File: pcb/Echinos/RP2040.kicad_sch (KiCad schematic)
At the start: 30 parts, among them J2 TagConnect_6pins, SW1 SW_Push, SW2 SW_Push, U2 RP2040, U2 W25Q128JVS, X1 ASE-12MHz

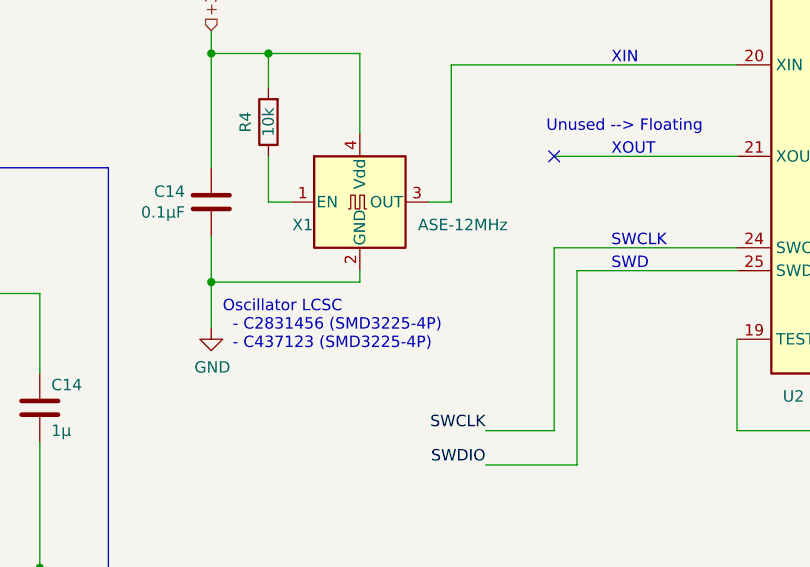
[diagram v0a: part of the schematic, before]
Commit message: ♻️ [PCB] - Fill / Check LCSC part number. Still some parts without a number:   - FPC connectors   - SATA connector   - Reset / Bootloader switches   - LED
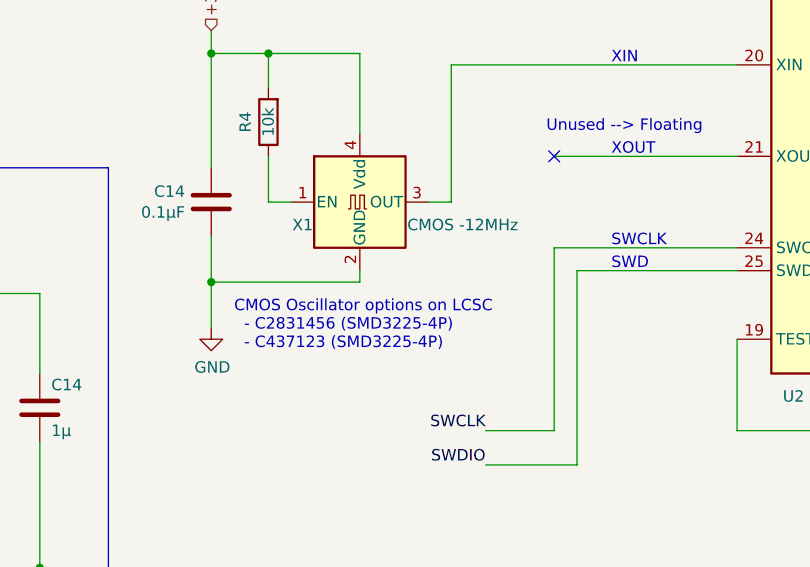
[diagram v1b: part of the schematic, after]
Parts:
- C14: LCSC TODO -> C5139511
- C14, C16: LCSC C19666 -> C458913
- R13: LCSC (none) -> C25744
- X1: value ASE-12MHz -> CMOS -12MHz; LCSC TODO -> C437123
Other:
- note added: "CMOS Oscillator options on LCSC - C2831456 (SMD3225-4P) - C437123 (SMD3225-4P)"
- note removed: "Oscillator LCSC - C2831456 (SMD3225-4P) - C437123 (SMD3225-4P)"
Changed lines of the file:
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@@
     (effects (font (size 1.27 1.27)) (justify right bottom))
   )
-  (text "Oscillator LCSC\n  - C2831456 (SMD3225-4P)\n  - C437123 (SMD3225-4P)"
-    (at 114.3 147.32 0)
+  (text "CMOS Oscillator options on LCSC\n  - C2831456 (SMD3225-4P)\n  - C437123 (SMD3225-4P)"
+    (at 115.57 147.32 0)
     (effects (font (size 1.27 1.27)) (justify left bottom))
   )
@@
       (effects (font (size 1.27 1.27)) hide)
     )
-    (property "LCSC" "C19666" (at 234.95 45.72 0)
+    (property "LCSC" "C458913" (at 234.95 45.72 0)
       (effects (font (size 1.27 1.27)) hide)
     )
@@
       (effects (font (size 1.27 1.27)) hide)
     )
-    (property "LCSC" "TODO" (at 113.03 130.81 0)
+    (property "LCSC" "C5139511" (at 113.03 130.81 0)
       (effects (font (size 1.27 1.27)) hide)
     )
@@
       (effects (font (size 1.27 1.27)) hide)
     )
-    (property "LCSC" "" (at 274.32 93.98 0)
+    (property "LCSC" "C25744" (at 274.32 93.98 0)
       (effects (font (size 1.27 1.27)) hide)
     )
@@
       (effects (font (size 1.27 1.27)) hide)
     )
-    (property "LCSC" "C19666" (at 170.18 46.99 0)
+    (property "LCSC" "C458913" (at 170.18 46.99 0)
       (effects (font (size 1.27 1.27)) hide)
     )
@@
       (effects (font (size 1.27 1.27)))
     )
-    (property "Value" "ASE-12MHz" (at 140.97 133.35 0)
+    (property "Value" "CMOS -12MHz" (at 140.97 133.35 0)
       (effects (font (size 1.27 1.27)))
     )
@@
       (effects (font (size 1.27 1.27)) hide)
     )
-    (property "Datasheet" "http://www.abracon.com/Oscillators/ASV.pdf" (at 127 130.81 0)
-      (effects (font (size 1.27 1.27)) hide)
-    )
-    (property "LCSC" "TODO" (at 129.54 130.81 0)
-      (effects (font (size 1.27 1.27)) hide)
-    )
+    (property "Datasheet" "https://datasheet.lcsc.com/lcsc/2304140030_JGHC-O3212000153350_C437123.pdf" (at 127 130.81 0)
+      (effects (font (size 1.27 1.27)) hide)
+    )
+    (property "LCSC" "C437123" (at 129.54 130.81 0)
+      (effects (font (size 1.27 1.27)) hide)
+    )

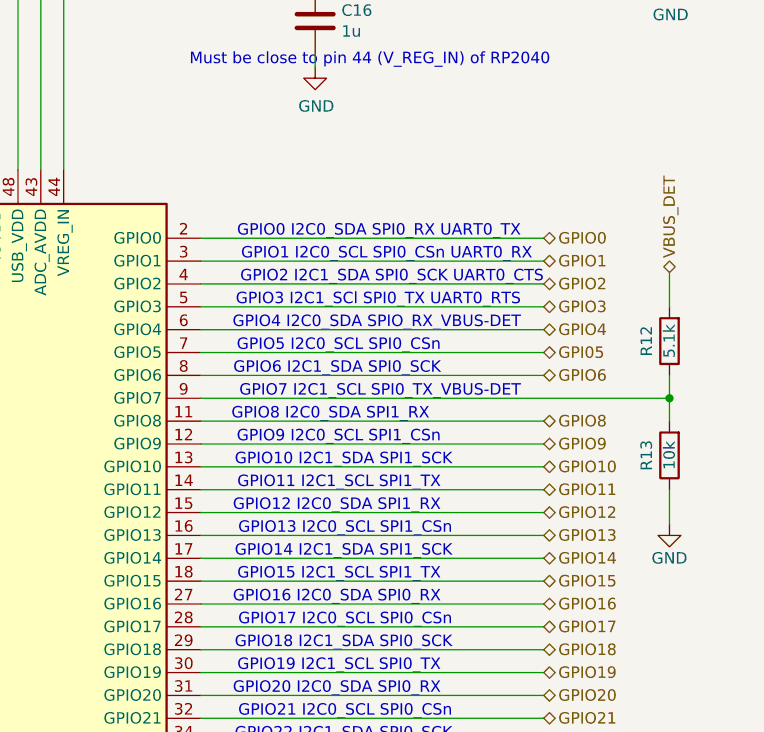
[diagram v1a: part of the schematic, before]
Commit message: 🚸 💥 🏗️ [PCB] - Start improving overall MCU routing to be able to make space for headers (SPI, Joystick, ...). USB + FLASH + VIK + DET + 5V --> 3.3V + ROW + COL
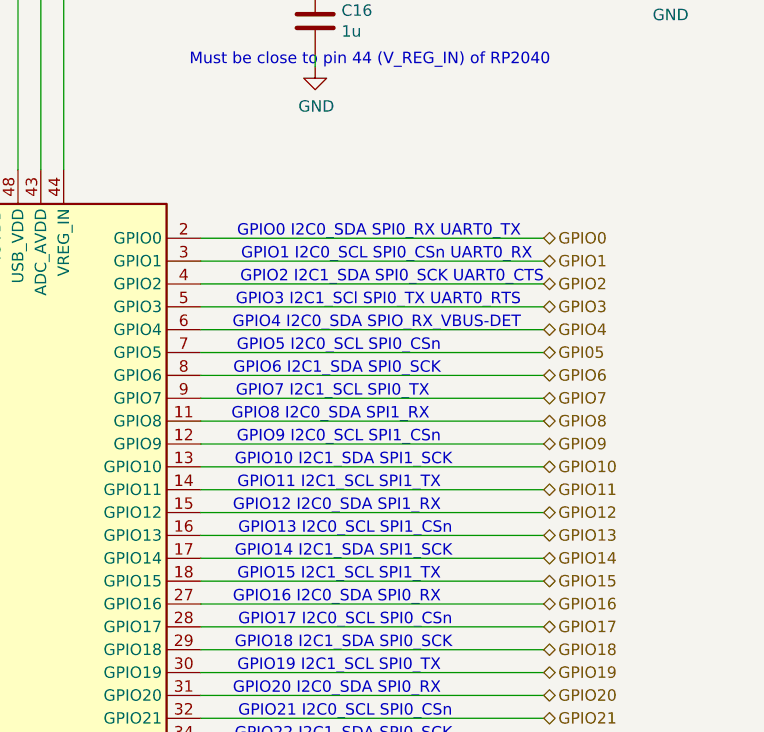
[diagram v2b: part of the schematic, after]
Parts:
- removed R12: 5.1k, Resistor_SMD:R_0402_1005Metric_Pad0.72x0.64mm_HandSolder, symbol Device:R
- removed R13: 10k, Resistor_SMD:R_0402_1005Metric_Pad0.72x0.64mm_HandSolder, symbol Device:R
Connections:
- net GPIO7: now reaches U2.9 (GPIO7)
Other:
- note added: "GPIO7 I2C1_SCL SPI0_TX"
- note removed: "GPIO7 I2C1_SCL SPI0_TX_VBUS-DET"
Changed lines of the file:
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@@
   (junction (at 130.81 83.82) (diameter 0) (color 0 0 0 0)
-  )
-  (junction (at 274.32 87.63) (diameter 0) (color 0 0 0 0)
   )
   (junction (at 119.38 114.3) (diameter 0) (color 0 0 0 0)
@@
     (stroke (width 0) (type default))
   )
-  (wire (pts (xy 222.25 87.63) (xy 274.32 87.63))
-    (stroke (width 0) (type default))
-  )
   (wire (pts (xy 222.25 115.57) (xy 260.35 115.57))
     (stroke (width 0) (type default))
@@
     (stroke (width 0) (type default))
   )
-  (wire (pts (xy 274.32 101.6) (xy 274.32 97.79))
-    (stroke (width 0) (type default))
-  )
   (wire (pts (xy 58.42 148.59) (xy 63.5 148.59))
     (stroke (width 0) (type default))
@@
     (stroke (width 0) (type default))
   )
-  (wire (pts (xy 274.32 85.09) (xy 274.32 87.63))
-    (stroke (width 0) (type default))
-  )
   (wire (pts (xy 170.18 50.8) (xy 170.18 52.07))
     (stroke (width 0) (type default))
@@
     (stroke (width 0) (type default))
   )
-  (wire (pts (xy 274.32 87.63) (xy 274.32 90.17))
-    (stroke (width 0) (type default))
-  )
   (wire (pts (xy 63.5 148.59) (xy 68.58 148.59))
     (stroke (width 0) (type default))
@@
     (stroke (width 0) (type default))
   )
+  (wire (pts (xy 222.25 87.63) (xy 260.35 87.63))
+    (stroke (width 0) (type default))
+  )
   (wire (pts (xy 204.47 41.91) (xy 204.47 62.23))
     (stroke (width 0) (type default))
@@
   )
   (wire (pts (xy 130.81 69.85) (xy 171.45 69.85))
-    (stroke (width 0) (type default))
-  )
-  (wire (pts (xy 274.32 73.66) (xy 274.32 77.47))
     (stroke (width 0) (type default))
   )
@@
     (effects (font (size 1.27 1.27)) (justify right bottom))
   )
-  (text "GPIO7 I2C1_SCL SPI0_TX_VBUS-DET" (at 257.81 87.63 0)
+  (text "GPIO7 I2C1_SCL SPI0_TX" (at 247.65 87.63 0)
     (effects (font (size 1.27 1.27)) (justify right bottom))
   )
@@
     (effects (font (size 1.27 1.27) (color 0 132 132 1)) (justify left))
   )
+  (hierarchical_label "GPIO7" (shape bidirectional) (at 260.35 87.63 0) (fields_autoplaced)
+    (effects (font (size 1.27 1.27) (color 0 132 132 1)) (justify left))
+  )
   (hierarchical_label "GPIO15" (shape bidirectional) (at 260.35 107.95 0) (fields_autoplaced)
     (effects (font (size 1.27 1.27) (color 0 132 132 1)) (justify left))
@@
   )
   (hierarchical_label "GPIO10" (shape bidirectional) (at 260.35 95.25 0) (fields_autoplaced)
-    (effects (font (size 1.27 1.27) (color 0 132 132 1)) (justify left))
-  )
-  (hierarchical_label "VBUS_DET" (shape bidirectional) (at 274.32 73.66 90) (fields_autoplaced)
     (effects (font (size 1.27 1.27) (color 0 132 132 1)) (justify left))
   )
@@
         (path "/5bd3006d-ec09-4ffb-bec3-03fa5613b46a/82089e05-aeac-4bc0-b466-29ce28ef1ab1/c4049032-4686-4159-8189-d0ee5e6ce1e0"
           (reference "C1") (unit 1)
-        )
-      )
-    )
-  )
-  (symbol (lib_id "Device:R") (at 274.32 93.98 180) (unit 1)
-    (in_bom yes) (on_board yes) (dnp no)
-    (property "Reference" "R13" (at 271.78 93.98 90)
-      (effects (font (size 1.27 1.27)))
-    )
-    (property "Value" "10k" (at 274.32 93.98 90)
-      (effects (font (size 1.27 1.27)))
-    )
-    (property "Footprint" "Resistor_SMD:R_0402_1005Metric_Pad0.72x0.64mm_HandSolder" (at 276.098 93.98 90)
-      (effects (font (size 1.27 1.27)) hide)
-    )
-    (property "Datasheet" "~" (at 274.32 93.98 0)
-      (effects (font (size 1.27 1.27)) hide)
-    )
-    (property "LCSC" "C25744" (at 274.32 93.98 0)
-      (effects (font (size 1.27 1.27)) hide)
-    )
-    (pin "1")
-    (pin "2")
-    (instances
-      (project "Echinos"
-        (path "/5bd3006d-ec09-4ffb-bec3-03fa5613b46a/82089e05-aeac-4bc0-b466-29ce28ef1ab1/c4049032-4686-4159-8189-d0ee5e6ce1e0"
-          (reference "R13") (unit 1)
-        )
-      )
-    )
-  )
-  (symbol (lib_id "power:GND") (at 274.32 101.6 0) (unit 1)
-    (in_bom yes) (on_board yes) (dnp no)
-    (property "Reference" "#PWR0205" (at 274.32 107.95 0)
-      (effects (font (size 1.27 1.27)) hide)
-    )
-    (property "Value" "GND" (at 274.32 105.41 0)
-      (effects (font (size 1.27 1.27)))
-    )
-    (property "Footprint" "" (at 274.32 101.6 0)
-      (effects (font (size 1.27 1.27)) hide)
-    )
-    (property "Datasheet" "" (at 274.32 101.6 0)
-      (effects (font (size 1.27 1.27)) hide)
-    )
-    (pin "1")
-    (instances
-      (project "Echinos"
-        (path "/5bd3006d-ec09-4ffb-bec3-03fa5613b46a/82089e05-aeac-4bc0-b466-29ce28ef1ab1/c4049032-4686-4159-8189-d0ee5e6ce1e0"
-          (reference "#PWR0205") (unit 1)
-        )
-      )
-      (project "dilemma"
-        (path "/7353e96a-343a-4876-b497-b1d205a14d97"
-          (reference "#PWR0101") (unit 1)
         )
       )
@@
         )
       )
-    )
-  )
-  (symbol (lib_id "Device:R") (at 274.32 81.28 180) (unit 1)
-    (in_bom yes) (on_board yes) (dnp no)
-    (property "Reference" "R12" (at 271.78 81.28 90)
-      (effects (font (size 1.27 1.27)))
-    )
-    (property "Value" "5.1k" (at 274.32 81.28 90)
-      (effects (font (size 1.27 1.27)))
-    )
-    (property "Footprint" "Resistor_SMD:R_0402_1005Metric_Pad0.72x0.64mm_HandSolder" (at 276.098 81.28 90)
-      (effects (font (size 1.27 1.27)) hide)
-    )
-    (property "Datasheet" "~" (at 274.32 81.28 0)
-      (effects (font (size 1.27 1.27)) hide)
-    )
-    (property "LCSC" "C25905" (at 274.32 81.28 0)
-      (effects (font (size 1.27 1.27)) hide)
-    )
-    (pin "1")
-    (pin "2")
-    (instances
-      (project "Echinos"
-        (path "/5bd3006d-ec09-4ffb-bec3-03fa5613b46a/82089e05-aeac-4bc0-b466-29ce28ef1ab1/c4049032-4686-4159-8189-d0ee5e6ce1e0"
-          (reference "R12") (unit 1)
-        )
-      )

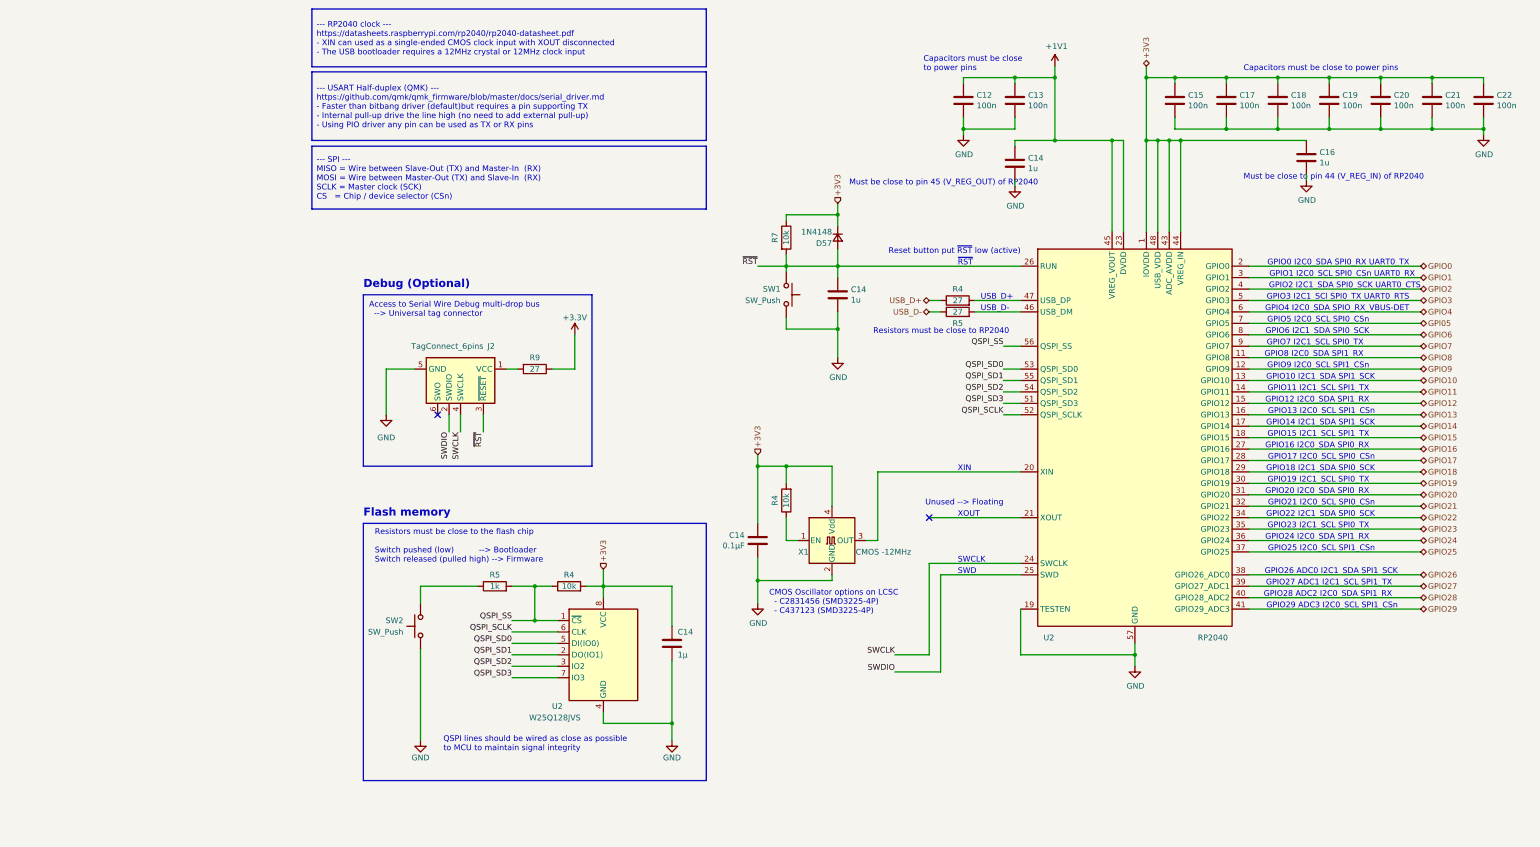
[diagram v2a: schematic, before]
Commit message: [PCB] - Save last state with in-board MCU.
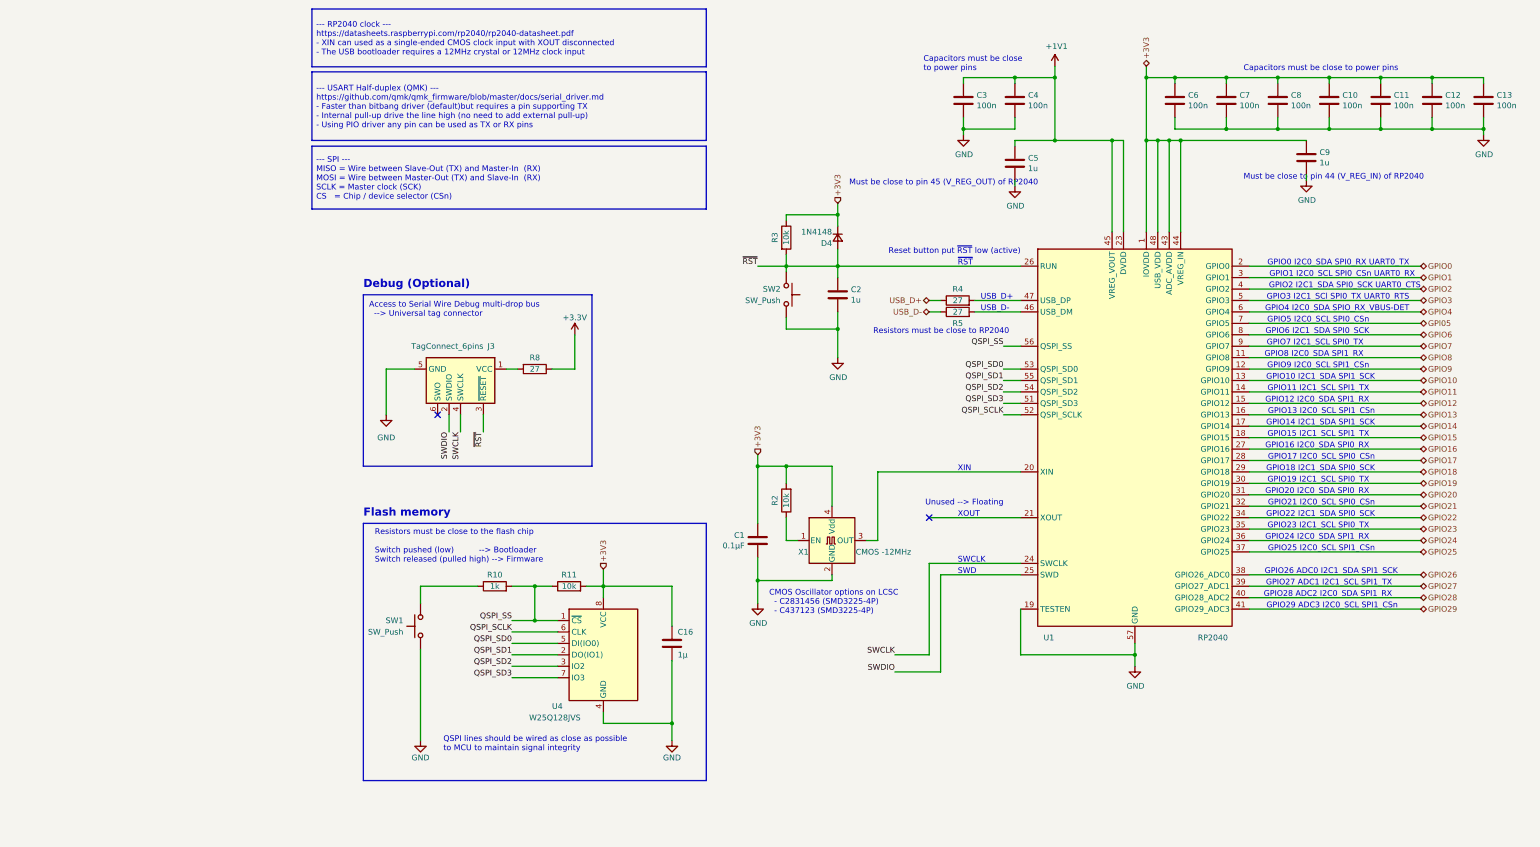
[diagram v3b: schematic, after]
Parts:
- renumbered C14 to C1, C19 to C10, C20 to C11, C21 to C12, C22 to C13, C14 to C16, C14 to C2, C12 to C3, C13 to C4, C14 to C5, C15 to C6, C17 to C7, C18 to C8, C16 to C9, D57 to D4, J2 to J3, R5 to R10, R4 to R11, R4 to R2, R7 to R3, R9 to R8, SW2 to SW1, SW1 to SW2, U2 to U1, U2 to U4

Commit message: [PCB] - Save last state with on board RP2040.
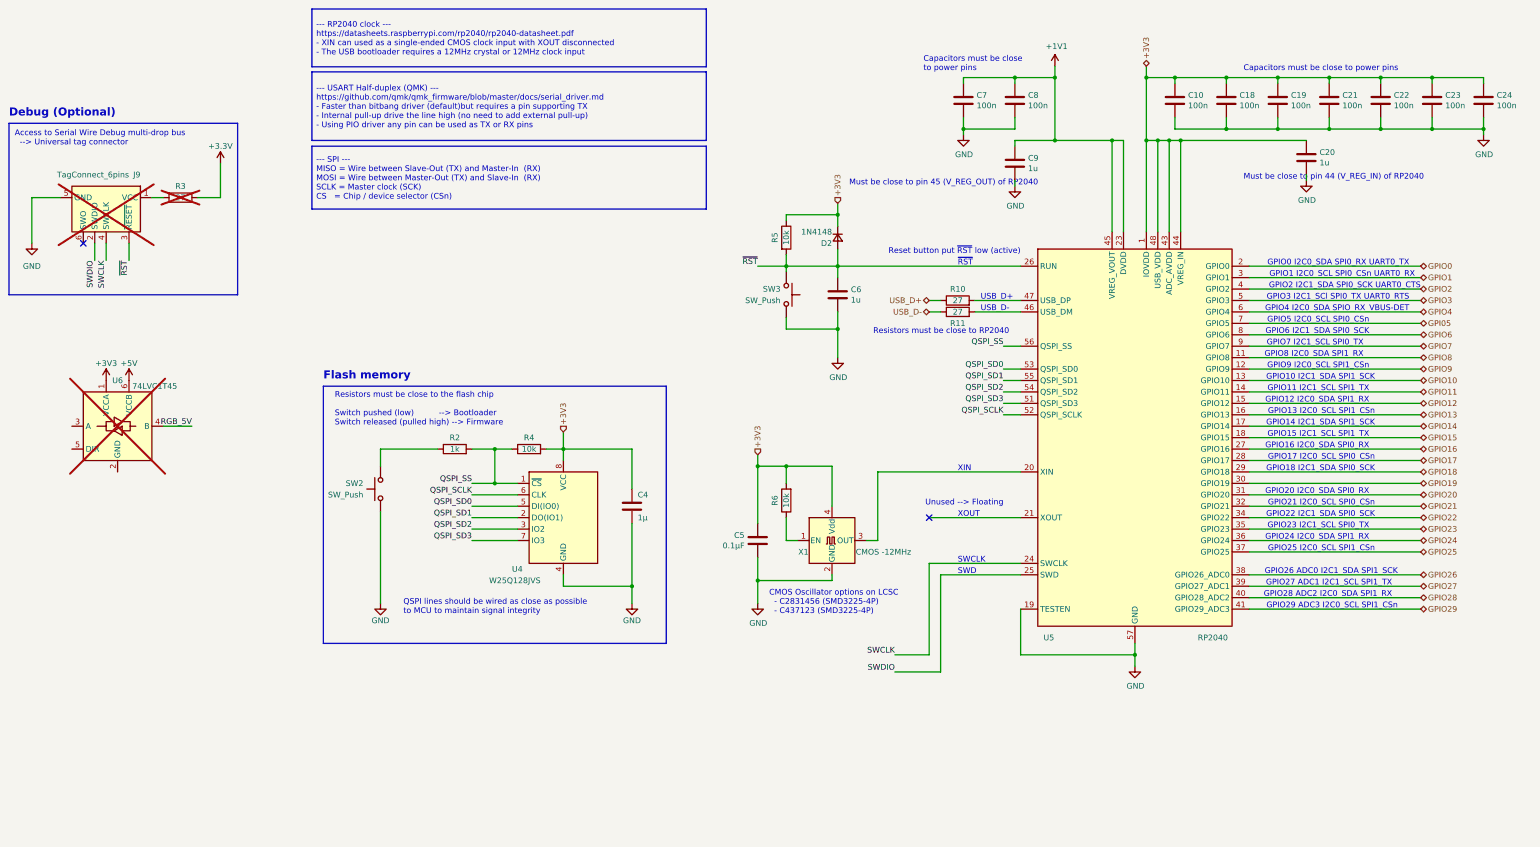
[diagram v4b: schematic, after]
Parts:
- added U6: 74LVC1T45, Package_TO_SOT_SMD:SOT-563, symbol Logic_LevelTranslator:SN74LVC1T45DRL
- J9: renamed from J3; now not fitted
- R3: renamed from R8; now not fitted; now left out of the parts list
- renumbered C6 to C10, C7 to C18, C8 to C19, C9 to C20, C10 to C21, C11 to C22, C12 to C23, C13 to C24, C16 to C4, C1 to C5, C2 to C6, C3 to C7, C4 to C8, C5 to C9, D4 to D2, R4 to R10, R5 to R11, R10 to R2, R11 to R4, R3 to R5, R2 to R6, SW1 to SW2, SW2 to SW3, U1 to U5
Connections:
- net +3V3: now also U6.1 (VCCA)
- new net +5V: U6.6 (VCCB)
- new net RGB_5V: U6.4 (B)
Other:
- note removed: "GPIO19 I2C1_SCL SPI0_TX"
- moved on the sheet: C4, R2, R4, SW2, U4
